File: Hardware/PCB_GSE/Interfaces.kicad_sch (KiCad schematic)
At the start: 32 parts, among them J3 GT17HN-4DP-2HA56, J4 Screw_Terminal_01x06, J5 Conn_02x10_Top_Bottom, J6 Conn_01x02, U5 SI5442DU-T1-GE3, U6 SI5442DU-T1-GE3, U7 SI5442DU-T1-GE3, U8 ISOW1044

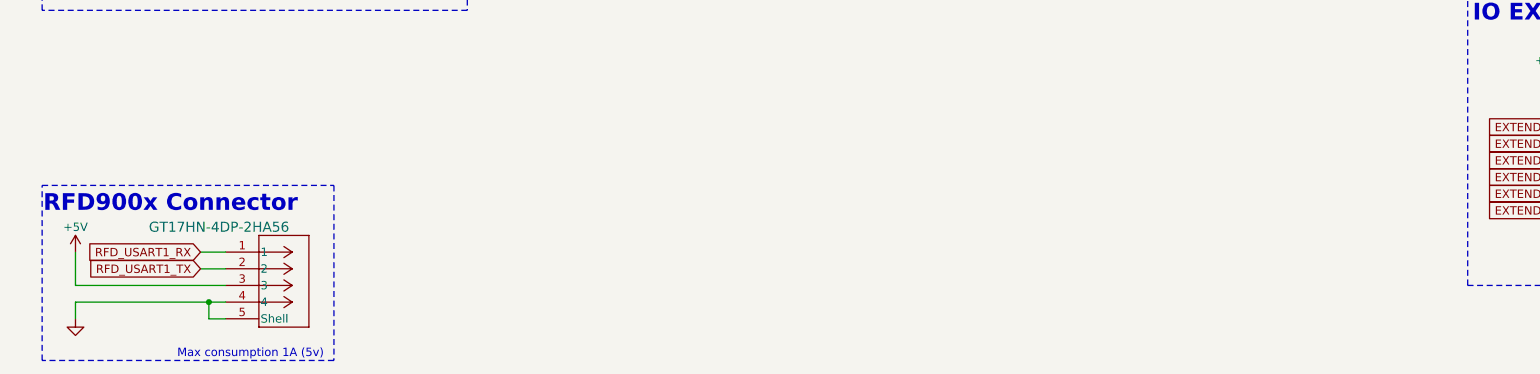
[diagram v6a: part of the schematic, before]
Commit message: fix: decoupling 3v3 missing
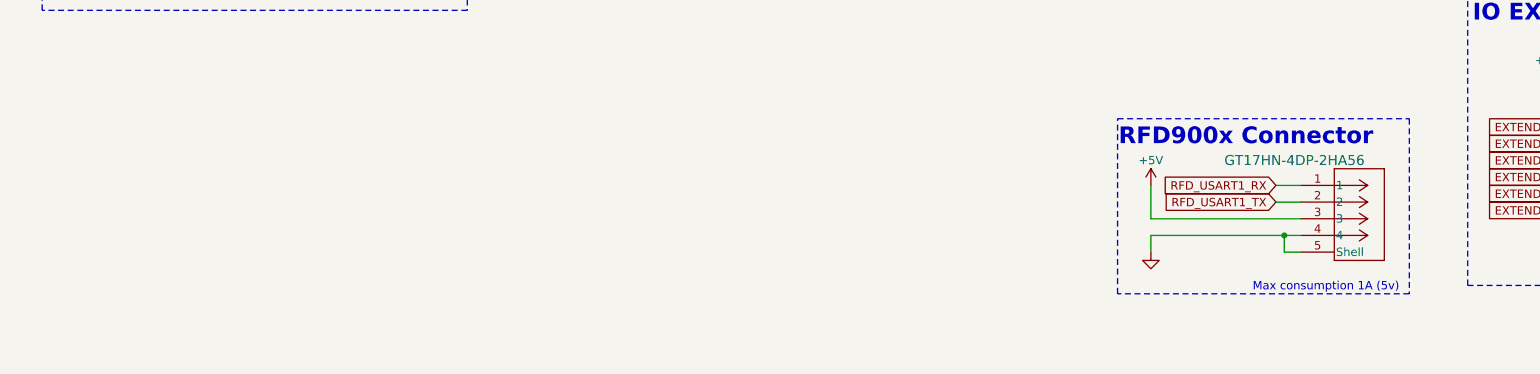
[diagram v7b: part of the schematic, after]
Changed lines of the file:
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@@
 	)
 	(rectangle
-		(start 13.97 148.59)
-		(end 58.42 175.26)
+		(start 177.8 138.43)
+		(end 222.25 165.1)
 		(stroke
 			(width 0)
@@
 	(text "Max consumption 1A (5v)"
 		(exclude_from_sim no)
-		(at 45.72 174.244 0)
+		(at 209.55 164.084 0)
 		(effects
 			(font
@@
 	(text "RFD900x Connector"
 		(exclude_from_sim no)
-		(at 33.528 151.384 0)
+		(at 197.358 141.224 0)
 		(effects
 			(font
@@
 	)
 	(junction
-		(at 39.37 166.37)
+		(at 203.2 156.21)
 		(diameter 0)
 		(color 0 0 0 0)
@@
 	(wire
 		(pts
-			(xy 39.37 168.91) (xy 39.37 166.37)
+			(xy 203.2 158.75) (xy 203.2 156.21)
 		)
 		(stroke
@@
 	(wire
 		(pts
-			(xy 38.1 158.75) (xy 41.91 158.75)
+			(xy 201.93 148.59) (xy 205.74 148.59)
 		)
 		(stroke
@@
 	(wire
 		(pts
-			(xy 39.37 166.37) (xy 19.05 166.37)
+			(xy 203.2 156.21) (xy 182.88 156.21)
 		)
 		(stroke
@@
 	(wire
 		(pts
-			(xy 41.91 166.37) (xy 39.37 166.37)
+			(xy 205.74 156.21) (xy 203.2 156.21)
 		)
 		(stroke
@@
 	(wire
 		(pts
-			(xy 19.05 163.83) (xy 41.91 163.83)
+			(xy 182.88 153.67) (xy 205.74 153.67)
 		)
 		(stroke
@@
 	(wire
 		(pts
-			(xy 38.1 161.29) (xy 41.91 161.29)
+			(xy 201.93 151.13) (xy 205.74 151.13)
 		)
 		(stroke
@@
 	(wire
 		(pts
-			(xy 19.05 166.37) (xy 19.05 168.91)
+			(xy 182.88 156.21) (xy 182.88 158.75)
 		)
 		(stroke
@@
 	(wire
 		(pts
-			(xy 41.91 168.91) (xy 39.37 168.91)
+			(xy 205.74 158.75) (xy 203.2 158.75)
 		)
 		(stroke
@@
 	(wire
 		(pts
-			(xy 19.05 158.75) (xy 19.05 163.83)
+			(xy 182.88 148.59) (xy 182.88 153.67)
 		)
 		(stroke
@@
 	(global_label "RFD_USART1_RX"
 		(shape input)
-		(at 38.1 158.75 180)
+		(at 201.93 148.59 180)
 		(fields_autoplaced yes)
 		(effects
@@
 		)
 		(property "Intersheetrefs" "${INTERSHEET_REFS}"
-			(at 19.9958 158.75 0)
+			(at 183.8258 148.59 0)
 			(effects
 				(font
@@
 	(global_label "RFD_USART1_TX"
 		(shape input)
-		(at 38.1 161.29 180)
+		(at 201.93 151.13 180)
 		(fields_autoplaced yes)
 		(effects
@@
 		)
 		(property "Intersheetrefs" "${INTERSHEET_REFS}"
-			(at 20.2982 161.29 0)
+			(at 184.1282 151.13 0)
 			(effects
 				(font
@@
 	(symbol
 		(lib_id "PCB_GSE:GT17HN-4DP-2HA56")
-		(at 41.91 158.75 0)
+		(at 205.74 148.59 0)
 		(unit 1)
 		(exclude_from_sim no)
@@
 		(dnp no)
 		(property "Reference" "J3"
-			(at 50.8 152.4 0)
+			(at 214.63 142.24 0)
 			(effects
 				(font
@@
 		)
 		(property "Value" "GT17HN-4DP-2HA56"
-			(at 30.226 154.94 0)
+			(at 194.056 144.78 0)
 			(effects
 				(font
@@
 		)
 		(property "Footprint" "CONN4_GT17HN_HIR"
-			(at 40.386 150.114 0)
+			(at 204.216 139.954 0)
 			(effects
 				(font
@@
 		)
 		(property "Datasheet" "GT17HN-4DP-2HA56"
-			(at 41.148 148.336 0)
+			(at 204.978 138.176 0)
 			(effects
 				(font
@@
 		)
 		(property "Description" ""
-			(at 41.91 158.75 0)
+			(at 205.74 148.59 0)
 			(effects
 				(font
@@
 	(symbol
 		(lib_id "power:+5V")
-		(at 19.05 158.75 0)
+		(at 182.88 148.59 0)
 		(unit 1)
 		(exclude_from_sim no)
@@
 		(dnp no)
 		(property "Reference" "#PWR058"
-			(at 19.05 162.56 0)
+			(at 182.88 152.4 0)
 			(effects
 				(font
@@
 		)
 		(property "Value" "+5V"
-			(at 19.05 154.94 0)
+			(at 182.88 144.78 0)
 			(effects
 				(font
@@
 		)
 		(property "Footprint" ""
-			(at 19.05 158.75 0)
+			(at 182.88 148.59 0)
 			(effects
 				(font
@@
 		)
 		(property "Datasheet" ""
-			(at 19.05 158.75 0)
+			(at 182.88 148.59 0)
 			(effects
 				(font
@@
 		)
 		(property "Description" "Power symbol creates a global label with name \"+5V\""
-			(at 19.05 158.75 0)
+			(at 182.88 148.59 0)
 			(effects
 				(font
@@
 	(symbol
 		(lib_id "power:GND")
-		(at 19.05 168.91 0)
+		(at 182.88 158.75 0)
 		(unit 1)
 		(exclude_from_sim no)
@@
 		(fields_autoplaced yes)
 		(property "Reference" "#PWR059"
-			(at 19.05 175.26 0)
+			(at 182.88 165.1 0)
 			(effects
 				(font
@@
 		)
 		(property "Value" "GND"
-			(at 19.05 173.99 0)
+			(at 182.88 163.83 0)
 			(effects
 				(font
@@
 		)
 		(property "Footprint" ""
-			(at 19.05 168.91 0)
+			(at 182.88 158.75 0)
 			(effects
 				(font
@@
 		)
 		(property "Datasheet" ""
-			(at 19.05 168.91 0)
+			(at 182.88 158.75 0)
 			(effects
 				(font
@@
 		)
 		(property "Description" ""
-			(at 19.05 168.91 0)
+			(at 182.88 158.75 0)
 			(effects
 				(font

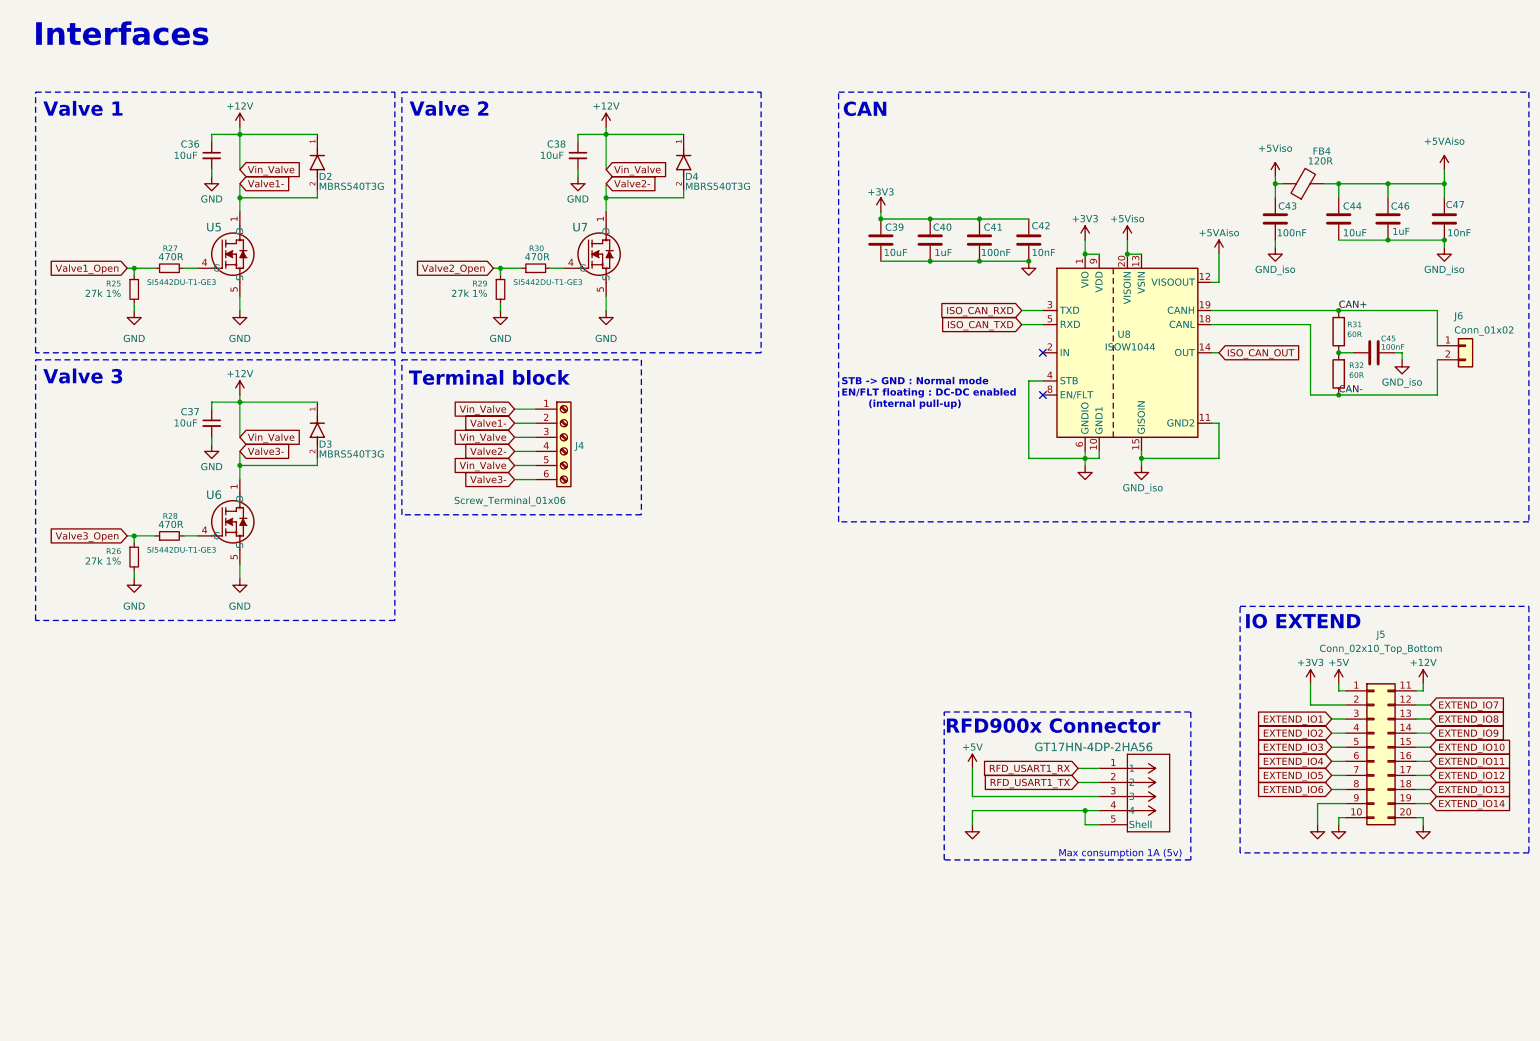
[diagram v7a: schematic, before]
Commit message: wip : Reduce BOM and fill all datasheet, digikey and MPN
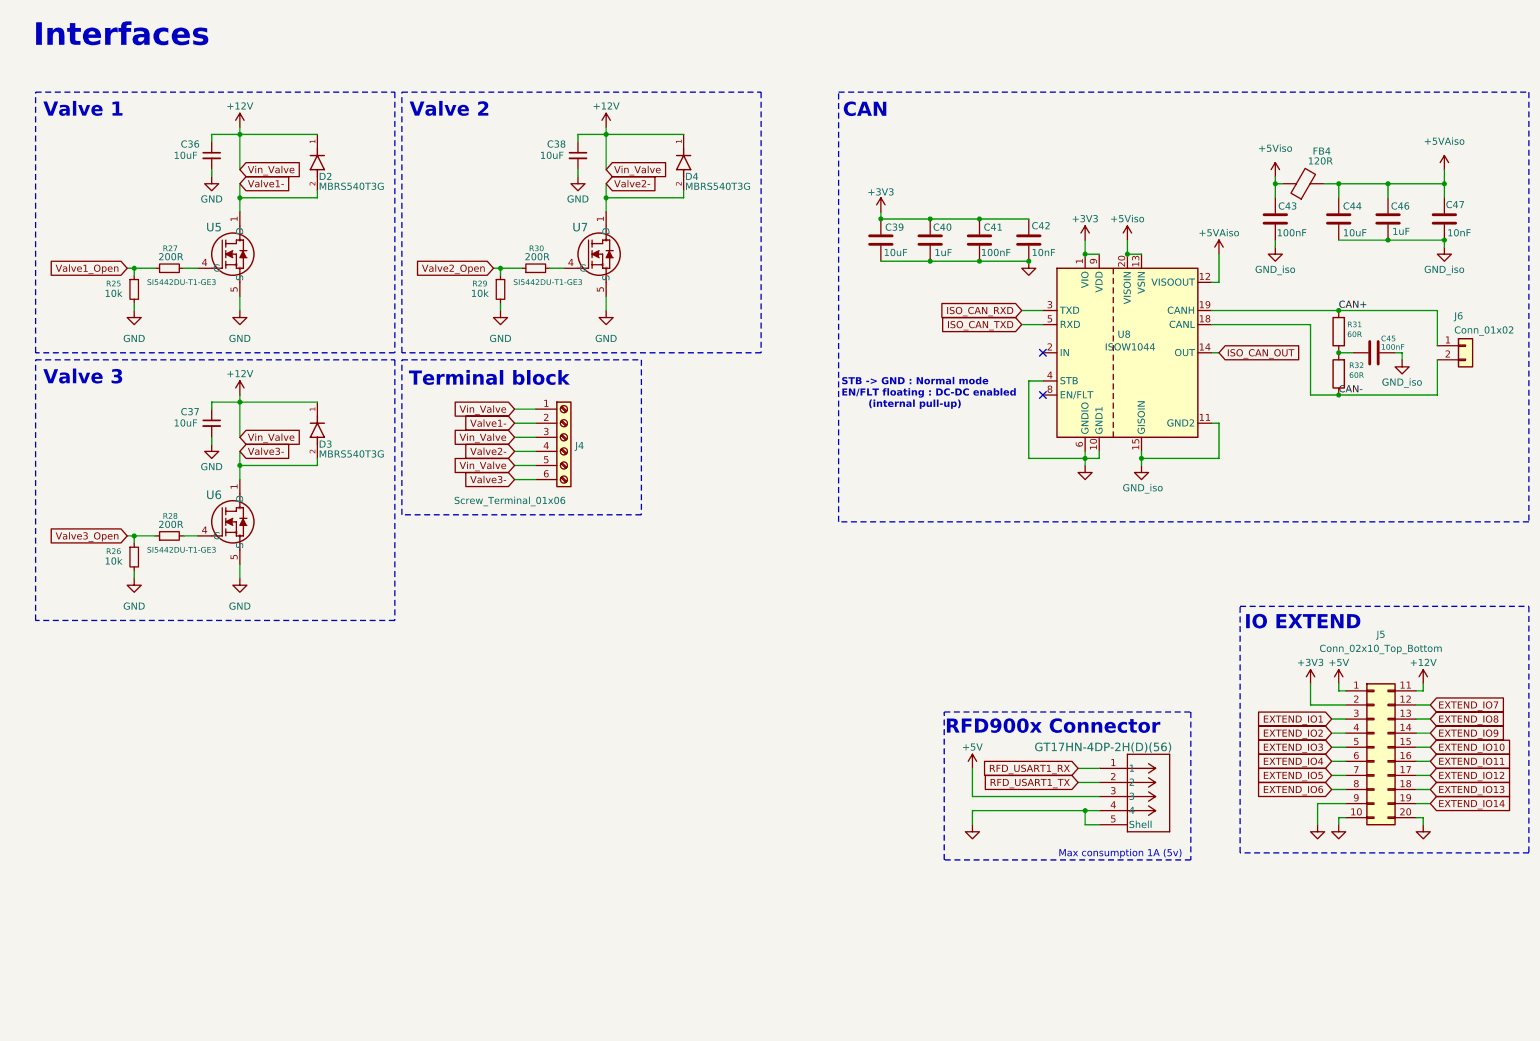
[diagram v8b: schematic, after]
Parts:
- C36, C37, C38: footprint Capacitor_SMD:C_0603_1608Metric -> Capacitor_SMD:C_0805_2012Metric; DigiKey_Part_Number 490-13248-1-ND -> 1276-2891-1-ND; Manufacturer_Part_Number GRM188R6YA106MA73D -> CL21A106KAYNNNE
- C39, C44: DigiKey_Part_Number (none) -> 1276-2891-1-ND; Manufacturer_Part_Number (none) -> CL21A106KAYNNNE
- C40, C46: DigiKey_Part_Number (none) -> 399-C0603C105K4RACTUCT-ND; Manufacturer_Part_Number (none) -> C0603C105K4RACTU
- C41, C43, C45: footprint Capacitor_SMD:C_0805_2012Metric -> Capacitor_SMD:C_0603_1608Metric; DigiKey_Part_Number (none) -> 399-C0603C104K3RACTUCT-ND; Manufacturer_Part_Number (none) -> C0603C104K3RACTU
- C42, C47: footprint Capacitor_SMD:C_0603_1608Metric -> Capacitor_SMD:C_0805_2012Metric; DigiKey_Part_Number (none) -> 1276-2434-1-ND; Manufacturer_Part_Number (none) -> CL21B103KAANNNC
- D2, D3, D4: footprint MBRS540T3G:DIOM7959X261N -> pcb_moteur:DIODE_SMB_2L_ONS; DigiKey_Part_Number MBRS540T3GOSCT-ND -> MBRS130LT3GOSCT-ND; Manufacturer_Part_Number (none) -> MBRS130LT3G
- FB4: DigiKey_Part_Number (none) -> 1934-1472-1-ND; Manufacturer_Part_Number (none) -> 2508051217Y6
- J3: value GT17HN-4DP-2HA56 -> GT17HN-4DP-2H(D)(56); footprint CONN4_GT17HN_HIR -> pcb_moteur:CONN4_GT17HN_HIR; DigiKey_Part_Number (none) -> 26-GT17HN-4DP-2H(D)(56)-ND; Manufacturer_Part_Number (none) -> GT17HN-4DP-2H(D)(56)
- J4: footprint (none) -> pcb_moteur:CONN_1725698_PXC; DigiKey_Part_Number (none) -> 277-1277-ND; Manufacturer_Part_Number (none) -> 1725698
- J5: DigiKey_Part_Number (none) -> 609-3221-ND; Manufacturer_Part_Number (none) -> 67996-420HLF
- J6: DigiKey_Part_Number (none) -> 900-2189890210CT-ND; Manufacturer_Part_Number (none) -> 2189890210
- R25, R26, R29: value 27k 1% -> 10k; footprint Resistor_SMD:R_0603_1608Metric -> Resistor_SMD:R_0805_2012Metric; DigiKey_Part_Number RG16P27.0KBCT-ND -> 311-10.0KHRCT-ND; Manufacturer_Part_Number RG1608P-273-B-T5 -> RC0603FR-0710KL
- R27, R28, R30: value 470R -> 200R; footprint Resistor_SMD:R_0603_1608Metric -> Resistor_SMD:R_0805_2012Metric; DigiKey_Part_Number 408-1766-1-ND -> YAG3707CT-ND; Manufacturer_Part_Number URG1608L-152-L-T05 -> AC0805FR-07200RL
- U5, U6, U7: footprint (none) -> pcb_moteur:SI5442DU_T1_G3; DigiKey_Part_Number (none) -> SI5442DU-T1-GE3CT-ND; Manufacturer_Part_Number (none) -> SI5442DU-T1-GE3
- U8: DigiKey_Part_Number (none) -> 296-ISOW1044BDFMRCT-ND; Manufacturer_Part_Number (none) -> ISOW1044BDFMR
